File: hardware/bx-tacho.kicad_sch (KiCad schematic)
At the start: 67 parts, among them J1 Conn_01x02, Q1 AO3401A, Q2 AO3401A, SW1 TS-1101-C-W, SW2 TS-1101-C-W, SW3 SK-12D02-G060, U1 ESP32-C3-WROOM-02, U2 TP4054_C5381776, U3 LMV393, U4 HS96L03W2C03

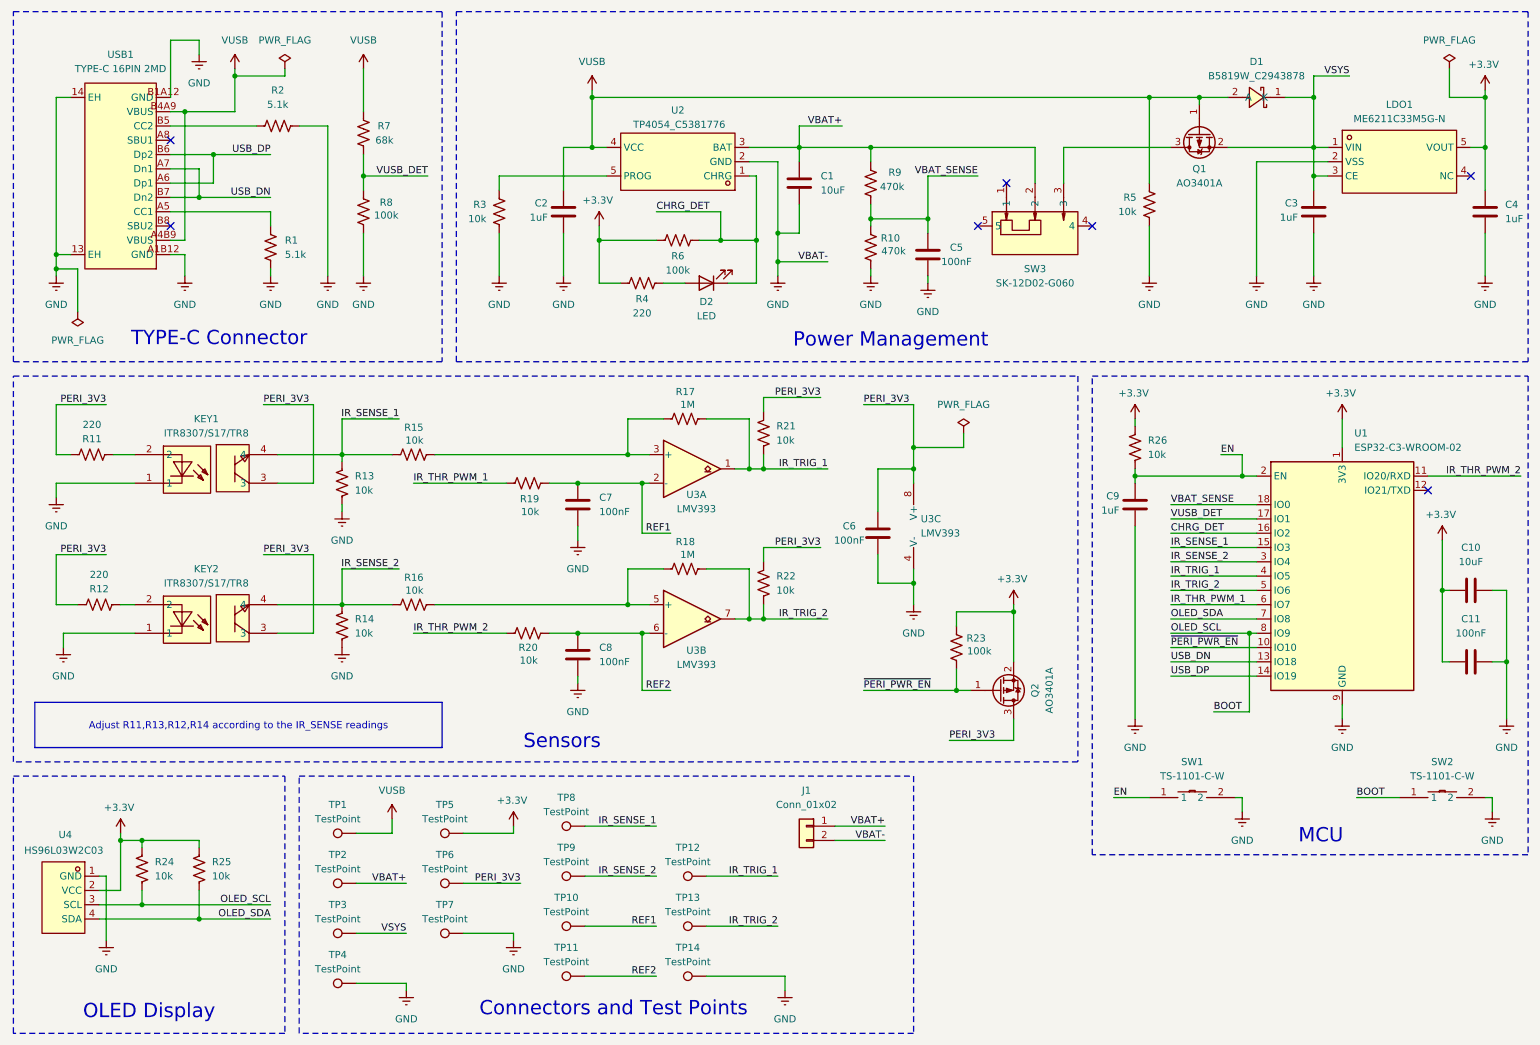
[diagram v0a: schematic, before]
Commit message: Finalize schematic for review (v0.2)
Schematic is complete and ready for PCB layout: every net traced, all
footprints assigned, R16 set to DNP, and PWR_FLAGs on VUSB, GND, +3V3
and RPM_CMP_PWR. Adds the LMV331 SOT-23-5 footprint and the custom
symbols it needs, and silences two noisy ERC checks (four_way_junction,
pin_to_pin) that only fire on expected topologies here.
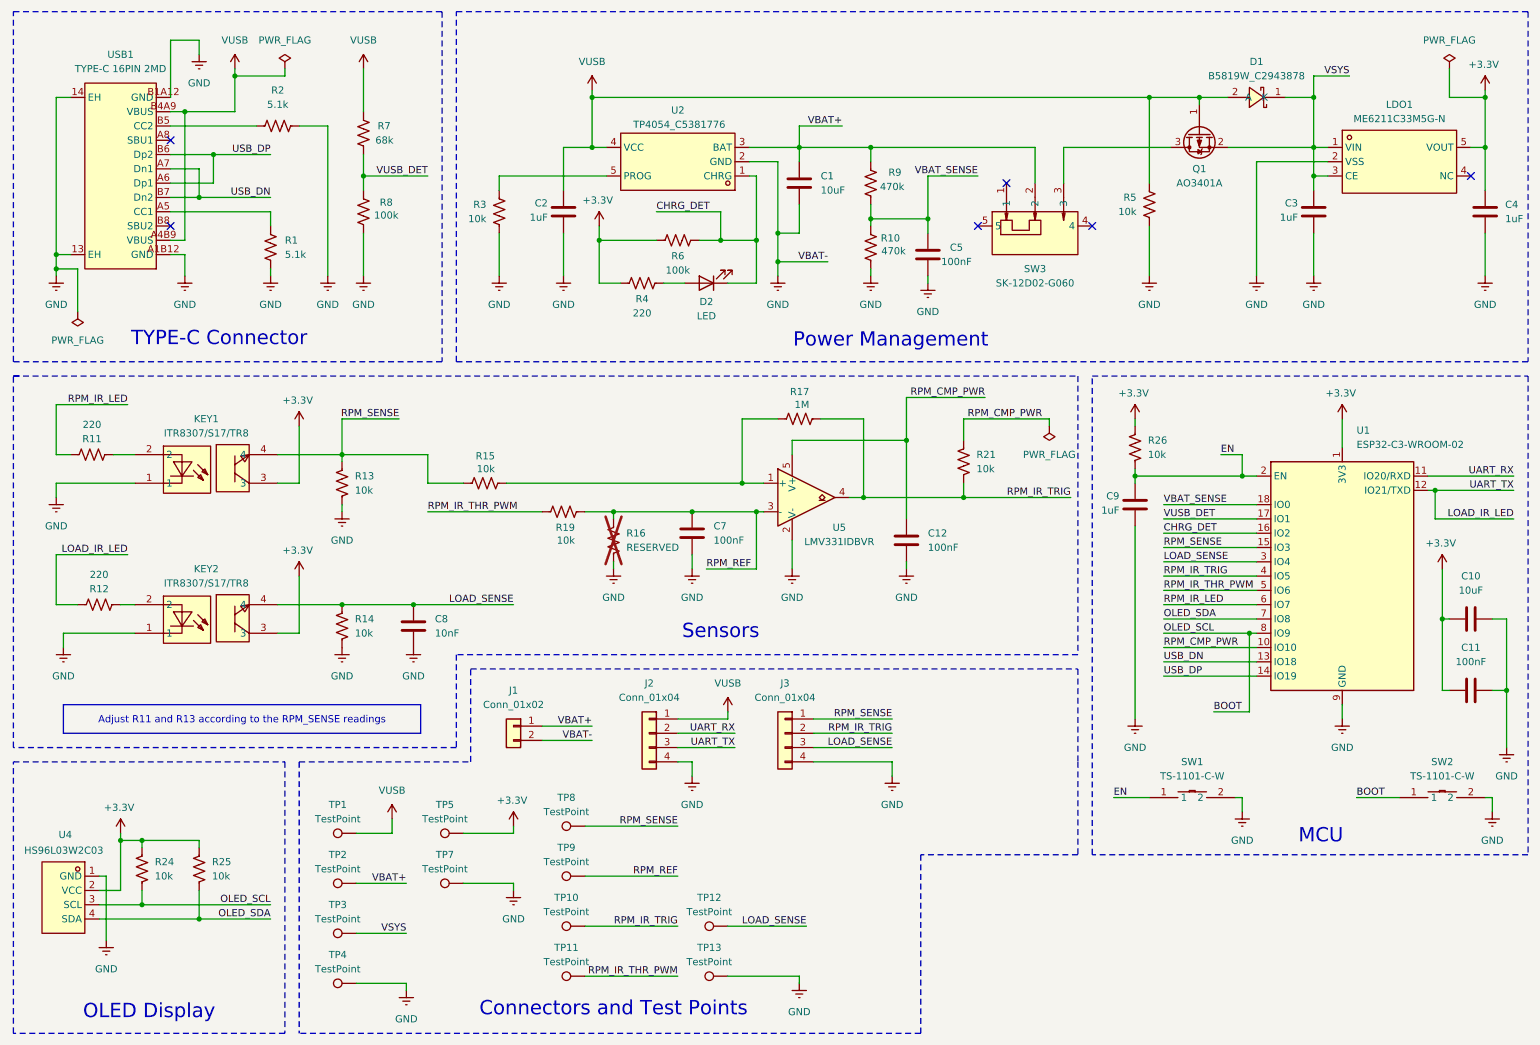
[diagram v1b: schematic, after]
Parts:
- removed C6: 100nF, Package_QFP:LQFP-100_14x14mm_P0.5mm, symbol Device:C
- removed Q2: AO3401A, Package_TO_SOT_SMD:SOT-23, symbol Transistor_FET:AO3401A
- removed R18: 1M, Package_DIP:DIP-8_W7.62mm, symbol Device:R_US
- removed R20, R22: 10k, Package_DIP:DIP-8_W7.62mm, symbol Device:R_US
- removed R23: 100k, Package_DIP:DIP-8_W7.62mm, symbol Device:R_US
- removed TP14, TP6: TestPoint, TestPoint:TestPoint_Pad_D1.5mm, symbol Connector:TestPoint
- removed U3: LMV393, lib:SOT-23-5_L2.9-W1.6-P0.95-LS2.8-BR, symbol Comparator:LMV393
- added C12: 100nF, Capacitor_SMD:C_0603_1608Metric, symbol Device:C
- added J2, J3: Conn_01x04, Connector_PinHeader_2.54mm:PinHeader_1x04_P2.54mm_Vertical, symbol Connector_Generic:Conn_01x04
- added U5: LMV331IDBVR, lib:SOT-23-5_L3.0-W1.7-P0.95-LS2.8-BR, symbol Comparator:LMV331
- C1, C10: footprint Package_QFP:LQFP-100_14x14mm_P0.5mm -> Capacitor_SMD:C_0805_2012Metric
- C11, C2, C3, C4, C5, C7, C9: footprint Package_QFP:LQFP-100_14x14mm_P0.5mm -> Capacitor_SMD:C_0603_1608Metric
- C8: value 100nF -> 10nF; footprint Package_QFP:LQFP-100_14x14mm_P0.5mm -> Capacitor_SMD:C_0603_1608Metric
- D2: footprint LED_SMD:LED_Cree-XHP50_3V_HighDensity -> LED_SMD:LED_0603_1608Metric_Pad1.05x0.95mm_HandSolder
- J1: footprint Package_SO:SOIC-8_3.9x4.9mm_P1.27mm -> Connector_Wire:SolderWire-0.15sqmm_1x02_P4mm_D0.5mm_OD1.5mm_Relief
- R1, R10, R11, R12, R13, R14, R15, R17, R19, R2, R21, R24, R25, R26, R3, R4, R5, R6, R7, R8, R9: footprint Package_DIP:DIP-8_W7.62mm -> Resistor_SMD:R_0603_1608Metric
- R16: value 10k -> RESERVED; footprint Package_DIP:DIP-8_W7.62mm -> Resistor_SMD:R_0603_1608Metric; now not fitted; now left out of the parts list
- TP1, TP10, TP11, TP12, TP13, TP2, TP3, TP4, TP5, TP7, TP8, TP9: footprint TestPoint:TestPoint_Pad_D1.5mm -> TestPoint:TestPoint_Pad_D1.0mm
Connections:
- net +3.3V: now also KEY1.3, KEY2.3
- net GND: now also R16.2, TP13.1, C12.2, J2.4 (Pin_4), J3.4 (Pin_4), U5.2 (V-)
- net VUSB: now also J2.1 (Pin_1)
- net RPM_REF: now reaches R16.1
- net RPM_REF: now also C7.1, R19.1, TP9.1, U5.3 (-)
- net LOAD_IR_LED: now reaches U1.12 (IO21/TXD)
- net LOAD_IR_LED: now also R12.2, J2.3 (Pin_3)
- net at R15.1, R17.2: now also U5.1 (+)
- net IR_SENSE_1 renamed RPM_SENSE
- net RPM_SENSE: now also J3.1 (Pin_1)
- net IR_SENSE_2 renamed LOAD_SENSE
- net LOAD_SENSE: now also C8.1, TP12.1, J3.3 (Pin_3); no longer R16.2, TP9.1
- net IR_THR_PWM_1 renamed RPM_IR_LED
- net RPM_IR_LED: now also R11.2; no longer R19.2
- net IR_THR_PWM_2 renamed UART_RX
- net UART_RX: now also J2.2 (Pin_2)
- net IR_TRIG_1 renamed RPM_IR_TRIG
- net RPM_IR_TRIG: now also TP10.1, J3.2 (Pin_2), U5.4; no longer TP12.1
- net IR_TRIG_2 renamed RPM_IR_THR_PWM
- net RPM_IR_THR_PWM: now also R19.2, TP11.1; no longer TP13.1
- removed net PERI_3V3: KEY1.3, KEY2.3, R11.2, R12.2, R21.1
- removed net REF1: C7.1, R19.1, TP10.1
- removed net REF2: C8.1, TP11.1
- net ~{PERI_PWR_EN} renamed RPM_CMP_PWR
- net RPM_CMP_PWR: now also R21.1, C12.1, U5.5 (V+)
- no-connect marks 7 -> 6
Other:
- moved on the sheet: C10, C11, C7, J1, R15, R17, R19, R21, TP12, TP13, TP7

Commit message: Start v0.2 PCB layout and add JLCPCB design rules
Work-in-progress layout:
- Import and place all 62 footprints; first routing pass and copper zones
- Add bx-tacho.kicad_dru with JLCPCB 2-layer, 1 oz fabrication limits
- Add custom BatteryPads_1x02_SMD_2x3mm_P4mm footprint (two 2x3 mm SMD
  pads, 4 mm pitch) and use it for J1 instead of the solder-wire footprint
- Export the BOM (bx-tacho.csv) and set up BOM fields in the project
- Add board-outline DXFs (plain, with mounting holes, with 2 mm mounting
  holes) for the Fusion 360 housing
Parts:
- J1: footprint Connector_Wire:SolderWire-0.15sqmm_1x02_P4mm_D0.5mm_OD1.5mm_Relief -> lib:BatteryPads_1x02_SMD_2x3mm_P4mm
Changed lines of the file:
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@@
 			)
 		)
-		(property "Footprint" "Connector_Wire:SolderWire-0.15sqmm_1x02_P4mm_D0.5mm_OD1.5mm_Relief"
+		(property "Footprint" "lib:BatteryPads_1x02_SMD_2x3mm_P4mm"
 			(at 102.87 140.97 0)
 			(hide yes)

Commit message: Complete v0.2 PCB layout and add fabrication outputs
Schematic:
- Remove test points TP1-TP13 and the J3 4-pin header
- Re-annotate components (reference designators renumbered)

PCB:
- Complete routing of all nets (0 unconnected items, schematic parity clean)
- Add 90ohm_diff net class for USB_DP/USB_DN
- Add curved teardrops on PTH pads, SMD pads and vias
- Convert USB1 and U4 mounting holes to NPTH; adjust USB1 GND pad
  position to meet JLC hole-to-copper clearance
- Tighten zone settings (0.2 mm min width, 0.3 mm thermal gap/spoke)
- Ignore courtyard-overlap and PTH-in-courtyard checks; exclude
  reviewed silkscreen and USB1 starved-thermal DRC items

Fabrication:
- Add Gerber and drill files plus bx-tacho-v0.2_gerber.zip for JLCPCB
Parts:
- removed J2: Conn_01x04, Connector_PinHeader_2.54mm:PinHeader_1x04_P2.54mm_Vertical, symbol Connector_Generic:Conn_01x04
- removed TP1, TP10, TP11, TP12, TP13, TP2, TP3, TP4, TP5, TP7, TP8, TP9: TestPoint, TestPoint:TestPoint_Pad_D1.0mm, symbol Connector:TestPoint
- renumbered C8 to C10, C9 to C6, C12 to C8, C10 to C9, J3 to J2, R2 to R1, R4 to R10, R17 to R11, R26 to R12, R11 to R13, R21 to R14, R13 to R15, R15 to R16, R19 to R17, R16 to R18, R12 to R19, R7 to R2, R14 to R20, R24 to R21, R25 to R22, R9 to R3, R5 to R4, R8 to R5, R3 to R6, R6 to R7, R1 to R8, R10 to R9, SW3 to SW1, SW1 to SW2, SW2 to SW3, U2 to U1, U5 to U2, U1 to U3
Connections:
- net +3.3V: no longer KEY1.3
- net LOAD_IR_LED: now also U3.6 (IO7); no longer U3.12 (IO21/TXD)
- net RPM_CMP_PWR: now also KEY1.3
- net RPM_IR_LED: now also U3.12 (IO21/TXD); no longer U3.6 (IO7)
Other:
- moved on the sheet: J1, J2

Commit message: Rework RPM sensor channel and fix layout review findings
Schematic (bench-validated on the v0.2 prototype, KEY1 = ITR8307/S17):
- R13 220 -> 100 ohm: more IR LED current
- R15 10k -> 22k: about 2.2x RPM_SENSE gain
- R11 1M -> 4.7M: hysteresis about 65 -> 22 mV
- New C12 2.2 nF across R15 to filter RPM_SENSE noise

PCB:
- Place C12 and rearrange C8, R11, R13-R16 around it
- Move vias out of the R13 and LDO1 pads
- Strengthen the USB1 GND pad connections (starved thermals)
- Add teardrops
- Update DRC exclusions in the project file
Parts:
- added C12: 2.2nF, Capacitor_SMD:C_0603_1608Metric, symbol Device:C
- R11: value 1M -> 4.7M
- R13: value 220 -> 100
- R15: value 10k -> 22k
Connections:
- net GND: now also C12.2
- net RPM_SENSE: now also C12.1
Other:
- moved on the sheet: R16
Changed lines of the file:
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@@
 	(title_block
 		(title "BX Tacho")
-		(date "2026-10-04")
-		(rev "v0.2")
+		(date "2026-10-17")
+		(rev "v1.0")
 	)
 	(rectangle
@@
 	)
 	(junction
+		(at 82.55 92.71)
+		(diameter 0)
+		(color 0 0 0 0)
+	)
+	(junction
 		(at 143.51 97.79)
 		(diameter 0)
@@
 	(wire
 		(pts
+			(xy 82.55 92.71) (xy 82.55 93.98)
+		)
+		(stroke
+			(width 0)
+			(type default)
+		)
+	)
+	(wire
+		(pts
 			(xy 111.76 38.1) (xy 116.84 38.1)
 		)
@@
 	(wire
 		(pts
-			(xy 87.63 92.71) (xy 87.63 97.79)
+			(xy 93.98 92.71) (xy 93.98 97.79)
 		)
 		(stroke
@@
 	(wire
 		(pts
-			(xy 87.63 97.79) (xy 93.98 97.79)
+			(xy 93.98 97.79) (xy 107.95 97.79)
 		)
 		(stroke
@@
 	(wire
 		(pts
+			(xy 82.55 92.71) (xy 93.98 92.71)
+		)
+		(stroke
+			(width 0)
+			(type default)
+		)
+	)
+	(wire
+		(pts
 			(xy 218.44 101.6) (xy 234.95 101.6)
 		)
@@
 	(wire
 		(pts
-			(xy 101.6 97.79) (xy 143.51 97.79)
+			(xy 115.57 97.79) (xy 143.51 97.79)
 		)
 		(stroke
@@
 		)
 	)
+	(wire
+		(pts
+			(xy 82.55 101.6) (xy 82.55 102.87)
+		)
+		(stroke
+			(width 0)
+			(type default)
+		)
+	)
 	(polyline
 		(pts
@@
 	(wire
 		(pts
-			(xy 72.39 92.71) (xy 87.63 92.71)
+			(xy 72.39 92.71) (xy 82.55 92.71)
 		)
 		(stroke
@@
 			)
 		)
-		(property "Value" "10k"
+		(property "Value" "22k"
 			(at 74.676 99.06 0)
 			(show_name no)
@@
 	)
 	(symbol
+		(lib_id "Device:C")
+		(at 82.55 97.79 0)
+		(unit 1)
+		(body_style 1)
+		(exclude_from_sim no)
+		(in_bom yes)
+		(on_board yes)
+		(in_pos_files yes)
+		(dnp no)
+		(fields_autoplaced yes)
+		(property "Reference" "C12"
+			(at 86.36 96.5199 0)
+			(show_name no)
+			(do_not_autoplace no)
+			(effects
+				(font
+					(size 1.27 1.27)
+				)
+				(justify left)
+			)
+		)
+		(property "Value" "2.2nF"
+			(at 86.36 99.0599 0)
+			(show_name no)
+			(do_not_autoplace no)
+			(effects
+				(font
+					(size 1.27 1.27)
+				)
+				(justify left)
+			)
+		)
+		(property "Footprint" "Capacitor_SMD:C_0603_1608Metric"
+			(at 83.5152 101.6 0)
+			(hide yes)
+			(show_name no)
+			(do_not_autoplace no)
+			(effects
+				(font
+					(size 1.27 1.27)
+				)
+			)
+		)
+		(property "Datasheet" ""
+			(at 82.55 97.79 0)
+			(hide yes)
+			(show_name no)
+			(do_not_autoplace no)
+			(effects
+				(font
+					(size 1.27 1.27)
+				)
+			)
+		)
+		(property "Description" "Unpolarized capacitor"
+			(at 82.55 97.79 0)
+			(hide yes)
+			(show_name no)
+			(do_not_autoplace no)
+			(effects
+				(font
+					(size 1.27 1.27)
+				)
+			)
+		)
+		(pin "1"
+		)
+		(pin "2"
+		)
+		(instances
+			(project "bx-tacho"
+				(path "/2c588408-32da-424d-a43f-d1ecf098f060"
+					(reference "C12")
+					(unit 1)
+				)
+			)
+		)
+	)
+	(symbol
 		(lib_id "power:GNDREF")
 		(at 100.33 60.96 0)
@@
 			)
 		)
-		(property "Value" "220"
+		(property "Value" "100"
 			(at 27.94 87.376 90)
 			(show_name no)
@@
 	)
 	(symbol
+		(lib_id "power:GNDREF")
+		(at 82.55 102.87 0)
+		(unit 1)
+		(body_style 1)
+		(exclude_from_sim no)
+		(in_bom yes)
+		(on_board yes)
+		(in_pos_files yes)
+		(dnp no)
+		(fields_autoplaced yes)
+		(property "Reference" "#PWR042"
+			(at 82.55 109.22 0)
+			(hide yes)
+			(show_name no)
+			(do_not_autoplace no)
+			(effects
+				(font
+					(size 1.27 1.27)
+				)
+			)
+		)
+		(property "Value" "GND"
+			(at 82.55 107.95 0)
+			(show_name no)
+			(do_not_autoplace no)
+			(effects
+				(font
+					(size 1.27 1.27)
+				)
+			)
+		)
+		(property "Footprint" ""
+			(at 82.55 102.87 0)
+			(hide yes)
+			(show_name no)
+			(do_not_autoplace no)
+			(effects
+				(font
+					(size 1.27 1.27)
+				)
+			)
+		)
+		(property "Datasheet" ""
+			(at 82.55 102.87 0)
+			(hide yes)
+			(show_name no)
+			(do_not_autoplace no)
+			(effects
+				(font
+					(size 1.27 1.27)
+				)
+			)
+		)
+		(property "Description" "Power symbol creates a global label with name \"GNDREF\" , reference supply ground"
+			(at 82.55 102.87 0)
+			(hide yes)
+			(show_name no)
+			(do_not_autoplace no)
+			(effects
+				(font
+					(size 1.27 1.27)
+				)
+			)
+		)
+		(pin "1"
+		)
+		(instances
+			(project "bx-tacho"
+				(path "/2c588408-32da-424d-a43f-d1ecf098f060"
+					(reference "#PWR042")
+					(unit 1)
+				)
+			)
+		)
+	)
+	(symbol
 		(lib_id "Device:R_US")
 		(at 153.67 86.36 270)
@@
 			)
 		)
-		(property "Value" "1M"
+		(property "Value" "4.7M"
 			(at 155.448 83.82 90)
 			(show_name no)
@@
 	(symbol
 		(lib_id "Device:R_US")
-		(at 97.79 97.79 270)
+		(at 111.76 97.79 270)
 		(unit 1)
 		(body_style 1)
@@
 		(dnp no)
 		(property "Reference" "R16"
-			(at 99.568 92.964 90)
+			(at 113.538 92.964 90)
 			(show_name no)
 			(do_not_autoplace no)
@@
 		)
 		(property "Value" "10k"
-			(at 99.568 95.25 90)
+			(at 113.538 95.25 90)
 			(show_name no)
 			(do_not_autoplace no)
@@
 		)
 		(property "Footprint" "Resistor_SMD:R_0603_1608Metric"
-			(at 97.536 98.806 90)
+			(at 111.506 98.806 90)
 			(hide yes)
 			(show_name no)
@@
 		)
 		(property "Datasheet" ""
-			(at 97.79 97.79 0)
+			(at 111.76 97.79 0)
 			(hide yes)
 			(show_name no)
@@
 		)
 		(property "Description" "Resistor, US symbol"
-			(at 97.79 97.79 0)
+			(at 111.76 97.79 0)
 			(hide yes)
 			(show_name no)

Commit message: Use 4.7k I2C pull-ups and run the OLED bus at 400 kHz
Hardware:
- R21/R22 (OLED SCL/SDA pull-ups) 10k -> 4.7k in schematic and PCB
- Teardrops regenerated on save; no routing or pour changes

Firmware:
- CONFIG_BXT_OLED_I2C_HZ default 100000 -> 400000; help text notes
  that 10k pull-ups still need 100 kHz
- A full frame now takes about 25 ms instead of about 95 ms

Tested on the v0.2 prototype with the reworked pull-ups.
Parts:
- R21, R22: value 10k -> 4.7k
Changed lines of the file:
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@@
 			)
 		)
-		(property "Value" "10k"
+		(property "Value" "4.7k"
 			(at 49.276 167.64 0)
 			(show_name no)
@@
 			)
 		)
-		(property "Value" "10k"
+		(property "Value" "4.7k"
 			(at 39.116 167.64 0)
 			(show_name no)

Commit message: Add LCSC part numbers for JLCPCB assembly
- LCSC field on every assembled part (47 of 50; J1/J2 hand-soldered,
  R18 DNP); D1 is now C8598 (JSCJ B5819W SL, JLCPCB Basic), with its
  value, MPN, manufacturer and old LCSC Part field updated to match in
  the schematic and the PCB
- Zones refilled (teardrops regenerated)
- Project DRC settings: silk-over-copper and library-footprint mismatch
  ignored, solder mask to copper clearance 0.005 mm, two stale
  starved-thermal exclusions removed
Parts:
- C1, C9: LCSC (none) -> C15850
- C10: LCSC (none) -> C57112
- C11, C5, C7, C8: LCSC (none) -> C14663
- C12: LCSC (none) -> C1604
- C2, C3, C4, C6: LCSC (none) -> C15849
- D1: value B5819W_C2943878 -> B5819W; LCSC (none) -> C8598; LCSC Part C2943878 -> C8598; MPN B5819W -> B5819W SL; Manufacturer GOODWORK(固得沃克) -> JSCJ
- D2: LCSC (none) -> C2286
- KEY1, KEY2: LCSC (none) -> C81632
- LDO1: LCSC (none) -> C82942
- Q1: LCSC (none) -> C15127
- R1, R8: LCSC (none) -> C23186
- R10, R19: LCSC (none) -> C22962
- R11: LCSC (none) -> C2930153
- R12, R14, R16, R17, R20, R4, R6: LCSC (none) -> C25804
- R13: LCSC (none) -> C22775
- R15: LCSC (none) -> C31850
- R2: LCSC (none) -> C23231
- R21, R22: LCSC (none) -> C23162
- R3, R9: LCSC (none) -> C23178
- R5, R7: LCSC (none) -> C25803
- SW1: LCSC (none) -> C2848884
- SW2, SW3: LCSC (none) -> C318938
- U1: LCSC (none) -> C5381776
- U2: LCSC (none) -> C34731
- U3: LCSC (none) -> C2934560
- U4: LCSC (none) -> C5248080
- USB1: LCSC (none) -> C2765186
